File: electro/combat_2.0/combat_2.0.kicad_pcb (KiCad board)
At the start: 2 copper layers, 110.7 x 51.6 mm, 50 parts, among them J1 BATT, J10 Conn_01x01_Pin, J11 Conn_01x01_Pin, J12 MOT_WPN, J13 Conn_02x09_Odd_Even, J14 Conn_02x09_Odd_Even, J2 Conn_01x02_Socket, J3 UART, J4 Conn_01x03_Pin, J5 Conn_01x03_Pin, J6 Conn_01x01_Pin, J7 Conn_01x01_Pin, J8 Conn_01x01_Pin, J9 Conn_01x01_Pin, Q1 AO4402G, Q2 AO4402G, Q3 AO4402G, Q4 AO4402G, SW1 EN, SW2 BOOT, U1 AZ1117CH-5.0TRG1, U2 LD29150DT33R, U3 TB6612FNG, U4 ACS712xLCTR-20A

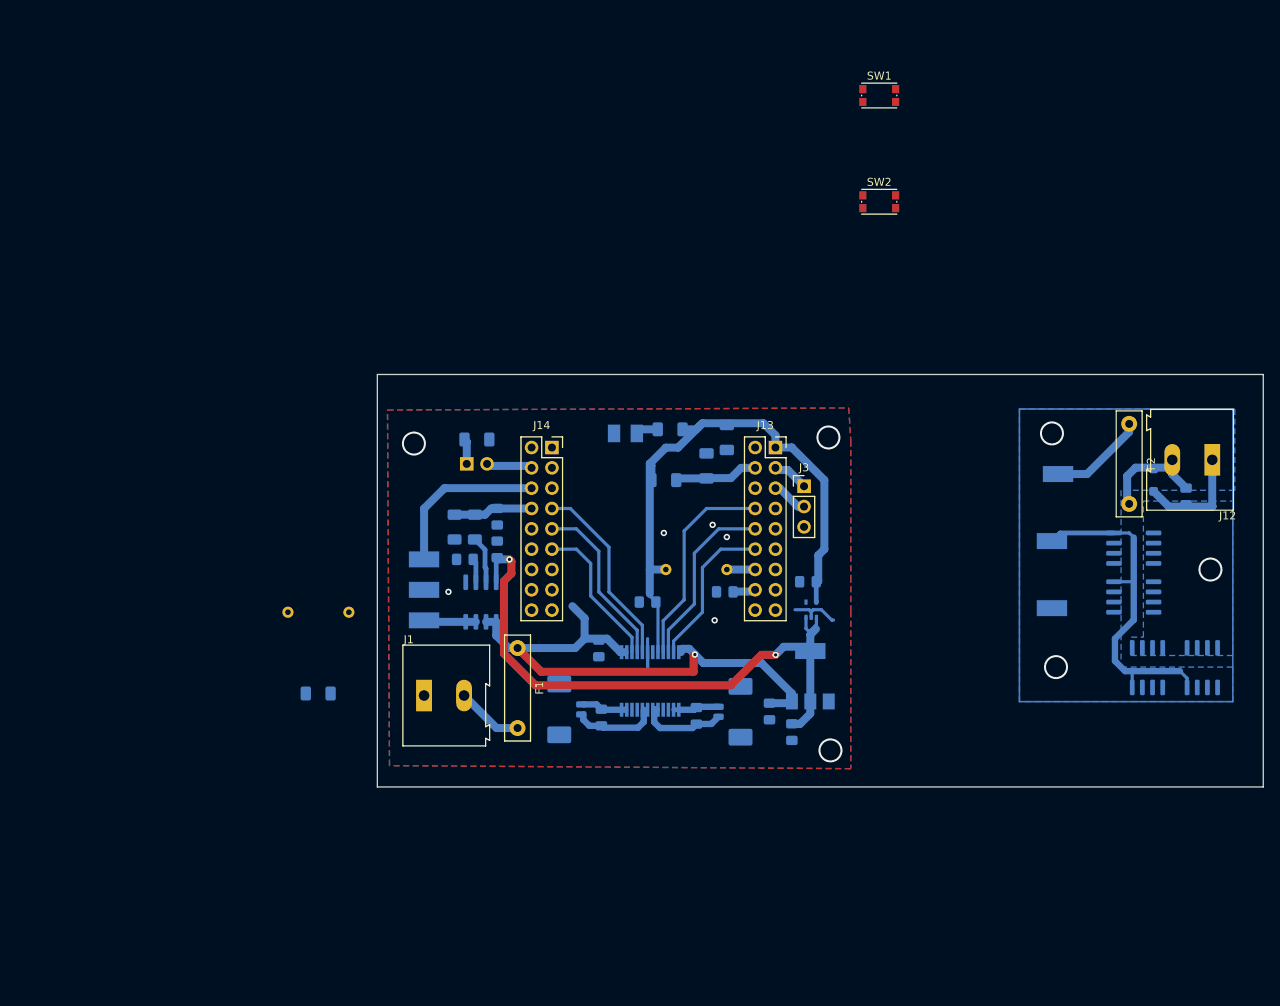
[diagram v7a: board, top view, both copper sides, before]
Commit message: Changed pads to ARKs (connecting two boards together), prepared for etching
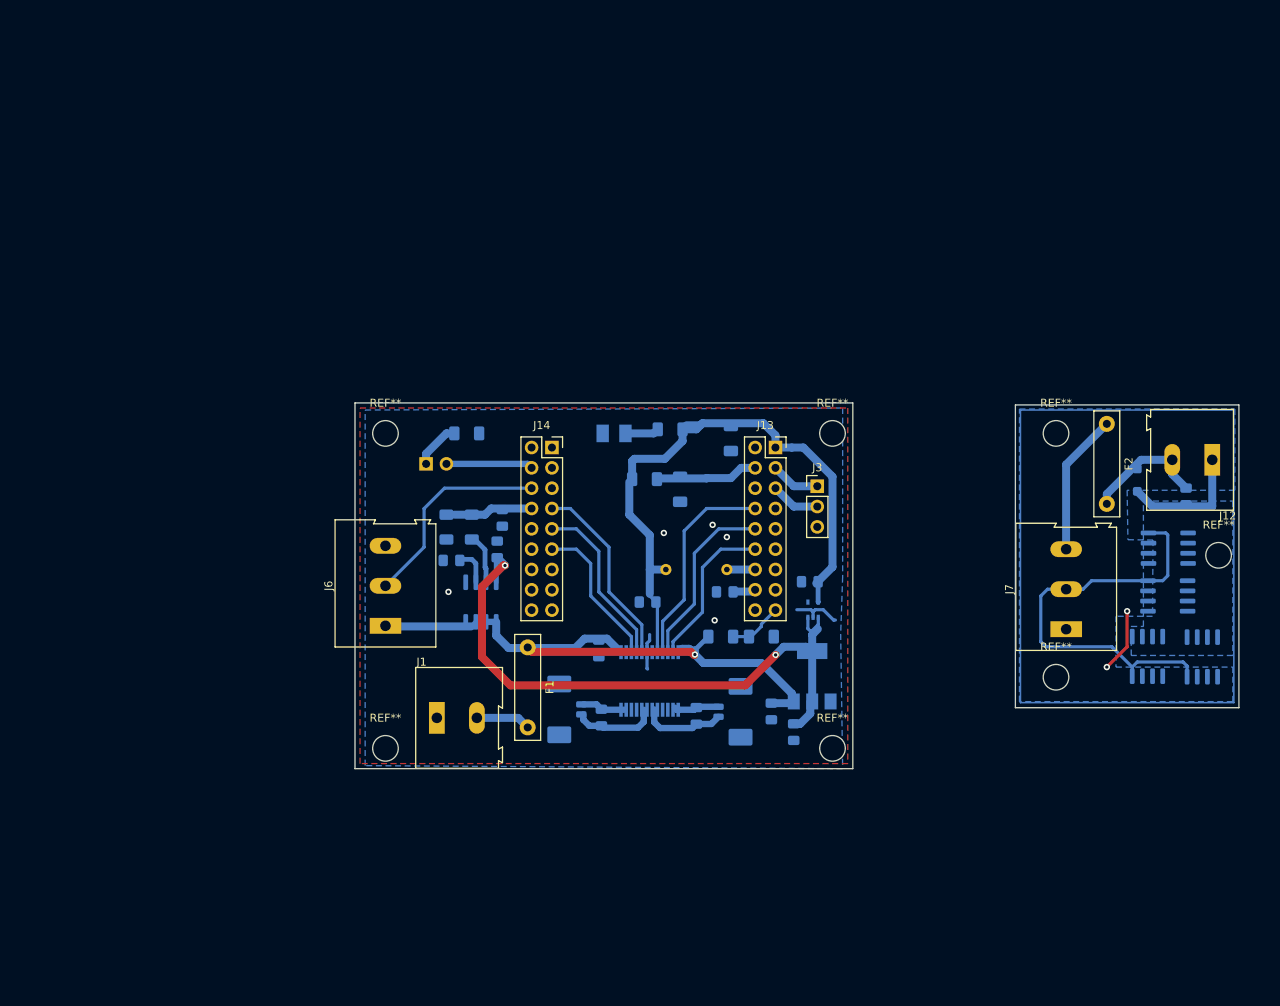
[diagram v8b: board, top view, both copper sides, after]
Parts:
- removed J10, J11, J8, J9: Conn_01x01_Pin, TestPoint:TestPoint_Keystone_5019_Minature
- removed SW1: EN, Button_Switch_SMD:SW_Push_1P1T_NO_CK_KMR2
- removed SW2: BOOT, Button_Switch_SMD:SW_Push_1P1T_NO_CK_KMR2
- added REF**: MountingHole_3.2mm_M3_DIN965, MountingHole:MountingHole_3.2mm_M3_DIN965, F.Cu at (113.0, 123.2)
- added REF**: MountingHole_3.2mm_M3_DIN965, MountingHole:MountingHole_3.2mm_M3_DIN965, F.Cu at (141.0, 83.8)
- added REF**: MountingHole_3.2mm_M3_DIN965, MountingHole:MountingHole_3.2mm_M3_DIN965, F.Cu at (161.3, 99.1)
- added REF**: MountingHole_3.2mm_M3_DIN965, MountingHole:MountingHole_3.2mm_M3_DIN965, F.Cu at (57.1, 123.2)
- added REF**: MountingHole_3.2mm_M3_DIN965, MountingHole:MountingHole_3.2mm_M3_DIN965, F.Cu at (141.0, 114.3)
- added REF**: MountingHole_3.2mm_M3_DIN965, MountingHole:MountingHole_3.2mm_M3_DIN965, F.Cu at (57.1, 83.8)
- added REF**: MountingHole_3.2mm_M3_DIN965, MountingHole:MountingHole_3.2mm_M3_DIN965, F.Cu at (113.0, 83.8)
- J6, J7: value Conn_01x01_Pin -> Conn_01x03_Socket; footprint TestPoint:TestPoint_Keystone_5019_Minature -> TerminalBlock:TerminalBlock_Altech_AK300-3_P5.00mm; moved to F.Cu
- R4: footprint Resistor_THT:R_Axial_DIN0204_L3.6mm_D1.6mm_P7.62mm_Horizontal -> Resistor_SMD:R_1206_3216Metric_Pad1.30x1.75mm_HandSolder
- moved J6 86.2 mm to (57.1, 107.9), turned to 90 degrees
- moved R5 55.9 mm to (104.1, 109.2), turned to 0 degrees
- moved R4 46.6 mm to (99.1, 109.2)
- moved J7 11.2 mm to (142.2, 108.3), turned to 90 degrees
- moved J2 5.08 mm to (62.2, 87.6)
- moved C1 4.41 mm to (94.0, 90.8), turned to 90 degrees
- moved Q4 4.32 mm to (155.0, 98.2)
- moved Q3 4.25 mm to (154.9, 104.1)
- moved J1 3.22 mm to (63.6, 119.4)
- moved F2 2.79 mm to (147.3, 82.6)
- moved R3 2.42 mm to (89.5, 89.5)
- moved D3 2.03 mm to (151.1, 89.7)
- moved C15 1.68 mm to (65.4, 99.7)
- moved J3 1.65 mm to (111.1, 90.4)
- moved R2 1.48 mm to (67.3, 83.8)
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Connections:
- J13 pad 17: /ESP32 PCB adapter/IO02 -> /BAT_LVL_ADC
- J7 pad 1: /PWM_WEAPON -> GND
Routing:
- net /PWM_WEAPON: track 63.8 -> 78.9 mm
- net /weapon_motor/MOTOR_PWR: track 18.6 -> 29.4 mm
- net /BAT_LVL_ADC: track 0.00 -> 6.83 mm
- net GND: track 12.2 -> 18.8 mm, vias 5 -> 7
- net +8V: track 71.3 -> 65.2 mm
- net /ESP32 PCB adapter/IO35: track 5.77 -> 10.9 mm
- net +5V: track 77.0 -> 79.8 mm
- net +3V3: track 74.0 -> 76.8 mm
- net Net-(J2-Pin_1): track 3.16 -> 5.85 mm
- net /ESP32 PCB adapter/EN: track 10.5 -> 12.9 mm
- net /weapon_motor/MOSFETS_DRAIN: track 14.0 -> 16.0 mm
- net /UART_TX: track 4.53 -> 6.18 mm
- net /UART_RX: track 4.53 -> 6.18 mm
- net Net-(U4-FILTER): track 3.00 -> 4.62 mm
- net Net-(J1-Pin_2): track 8.37 -> 6.84 mm
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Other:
- board size 110.7 x 51.6 mm -> 110.5 x 45.7 mm
